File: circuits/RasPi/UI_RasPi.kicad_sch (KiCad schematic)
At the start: 14 parts, among them Q30 BSS138, Q33 BSS138

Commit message: 更新
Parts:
- removed Q30, Q33: BSS138, Package_TO_SOT_SMD:SOT-23, symbol Device:Q_NMOS_GSD
- added Q23, Q24: 2N7002, Package_TO_SOT_SMD:SOT-23, symbol Transistor_FET:2N7002
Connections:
- net GNDD: now also Q23.2 (S), Q24.2 (S)
- net LED_nG0: now also Q24.1 (G)
- net LED_nR0: now also Q23.1 (G)
- net at D23.2 (A), R113.2: now also Q24.3 (D)
- net at D29.2 (A), R120.2: now also Q23.3 (D)
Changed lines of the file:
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@@
   (junction (at 147.32 106.68) (diameter 0) (color 0 0 0 0)
   )
+  (junction (at 132.08 111.76) (diameter 0) (color 0 0 0 0)
+  )
+  (junction (at 147.32 116.84) (diameter 0) (color 0 0 0 0)
+  )
   (junction (at 177.8 111.76) (diameter 0) (color 0 0 0 0)
-  )
-  (junction (at 147.32 116.84) (diameter 0) (color 0 0 0 0)
-  )
-  (junction (at 132.08 111.76) (diameter 0) (color 0 0 0 0)
   )
   (junction (at 193.04 116.84) (diameter 0) (color 0 0 0 0)
@@
     )
   )
+  (symbol (lib_id "Transistor_FET:2N7002") (at 137.16 111.76 0) (unit 1)
+    (in_bom yes) (on_board yes) (dnp no)
+    (property "Reference" "Q23" (at 129.54 104.14 0)
+      (effects (font (size 1.27 1.27)) (justify left))
+    )
+    (property "Value" "2N7002" (at 129.54 106.68 0)
+      (effects (font (size 1.27 1.27)) (justify left))
+    )
+    (property "Footprint" "Package_TO_SOT_SMD:SOT-23" (at 142.24 113.665 0)
+      (effects (font (size 1.27 1.27) italic) (justify left) hide)
+    )
+    (property "Datasheet" "https://www.onsemi.com/pub/Collateral/NDS7002A-D.PDF" (at 142.24 115.57 0)
+      (effects (font (size 1.27 1.27)) (justify left) hide)
+    )
+    (pin "3")
+    (pin "1")
+    (pin "2")
+    (instances
+      (project "RasPi"
+        (path "/689a9e74-f202-4ea4-bfbb-4341f2549250/fddad0c3-2af8-46e3-8794-fa1122d24d51/69fce92a-28f6-4191-9f2f-418081756bee"
+          (reference "Q23") (unit 1)
+        )
+      )
+    )
+  )
   (symbol (lib_id "Device:LED") (at 193.04 111.76 90) (unit 1)
     (in_bom yes) (on_board yes) (dnp no)
@@
         (path "/689a9e74-f202-4ea4-bfbb-4341f2549250/fddad0c3-2af8-46e3-8794-fa1122d24d51/69fce92a-28f6-4191-9f2f-418081756bee"
           (reference "R120") (unit 1)
-        )
-      )
-    )
-  )
-  (symbol (lib_name "Q_NMOS_GSD_1") (lib_id "Device:Q_NMOS_GSD") (at 182.88 111.76 0) (unit 1)
-    (in_bom yes) (on_board yes) (dnp no)
-    (property "Reference" "Q30" (at 180.34 116.84 0)
-      (effects (font (size 1.27 1.27)) (justify left))
-    )
-    (property "Value" "BSS138" (at 180.34 119.38 0)
-      (effects (font (size 1.27 1.27)) (justify left))
-    )
-    (property "Footprint" "Package_TO_SOT_SMD:SOT-23" (at 187.96 109.22 0)
-      (effects (font (size 1.27 1.27)) hide)
-    )
-    (property "Datasheet" "~" (at 182.88 111.76 0)
-      (effects (font (size 1.27 1.27)) hide)
-    )
-    (pin "1")
-    (pin "2")
-    (pin "3")
-    (instances
-      (project "RasPi"
-        (path "/689a9e74-f202-4ea4-bfbb-4341f2549250/fddad0c3-2af8-46e3-8794-fa1122d24d51/69fce92a-28f6-4191-9f2f-418081756bee"
-          (reference "Q30") (unit 1)
         )
       )
@@
     )
   )
+  (symbol (lib_id "Transistor_FET:2N7002") (at 182.88 111.76 0) (unit 1)
+    (in_bom yes) (on_board yes) (dnp no)
+    (property "Reference" "Q24" (at 175.26 104.14 0)
+      (effects (font (size 1.27 1.27)) (justify left))
+    )
+    (property "Value" "2N7002" (at 175.26 106.68 0)
+      (effects (font (size 1.27 1.27)) (justify left))
+    )
+    (property "Footprint" "Package_TO_SOT_SMD:SOT-23" (at 187.96 113.665 0)
+      (effects (font (size 1.27 1.27) italic) (justify left) hide)
+    )
+    (property "Datasheet" "https://www.onsemi.com/pub/Collateral/NDS7002A-D.PDF" (at 187.96 115.57 0)
+      (effects (font (size 1.27 1.27)) (justify left) hide)
+    )
+    (pin "3")
+    (pin "1")
+    (pin "2")
+    (instances
+      (project "RasPi"
+        (path "/689a9e74-f202-4ea4-bfbb-4341f2549250/fddad0c3-2af8-46e3-8794-fa1122d24d51/69fce92a-28f6-4191-9f2f-418081756bee"
+          (reference "Q24") (unit 1)
+        )
+      )
+    )
+  )
   (symbol (lib_id "Device:R") (at 154.94 139.7 270) (mirror x) (unit 1)
     (in_bom yes) (on_board yes) (dnp no)
@@
         )
       )
-    )
-  )
-  (symbol (lib_name "Q_NMOS_GSD_1") (lib_id "Device:Q_NMOS_GSD") (at 137.16 111.76 0) (unit 1)
-    (in_bom yes) (on_board yes) (dnp no)
-    (property "Reference" "Q33" (at 134.62 116.84 0)
-      (effects (font (size 1.27 1.27)) (justify left))
-    )
-    (property "Value" "BSS138" (at 134.62 119.38 0)
-      (effects (font (size 1.27 1.27)) (justify left))
-    )
-    (property "Footprint" "Package_TO_SOT_SMD:SOT-23" (at 142.24 109.22 0)
-      (effects (font (size 1.27 1.27)) hide)
-    )
-    (property "Datasheet" "~" (at 137.16 111.76 0)
-      (effects (font (size 1.27 1.27)) hide)
-    )
-    (pin "1")
-    (pin "2")
-    (pin "3")
-    (instances
-      (project "RasPi"
-        (path "/689a9e74-f202-4ea4-bfbb-4341f2549250/fddad0c3-2af8-46e3-8794-fa1122d24d51/69fce92a-28f6-4191-9f2f-418081756bee"
-          (reference "Q33") (unit 1)
-        )
-      )

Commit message: raspi基板回路図
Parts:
- added D19, D28: Blue, LED_SMD:LED_0603_1608Metric_Pad1.05x0.95mm_HandSolder, symbol Device:LED
- added H7, H8: MountingHole_Pad, TestPoint:TestPoint_Pad_1.0x1.0mm, symbol Mechanical:MountingHole_Pad
- added R3, R42: 1k, Resistor_SMD:R_0402_1005Metric, symbol Device:R
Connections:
- net GNDD: now also D19.1 (K), D28.1 (K)
- new net: D28.2 (A), R42.1
- new net: D19.2 (A), R3.1
- new net LED_B0: H7.1, R3.2
- new net LED_B1: H8.1, R42.2
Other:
- note added: "LED"
- moved on the sheet: D23, D24, D25, D26, D29, Q23, Q24, R110, R111, R112, R113, R114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

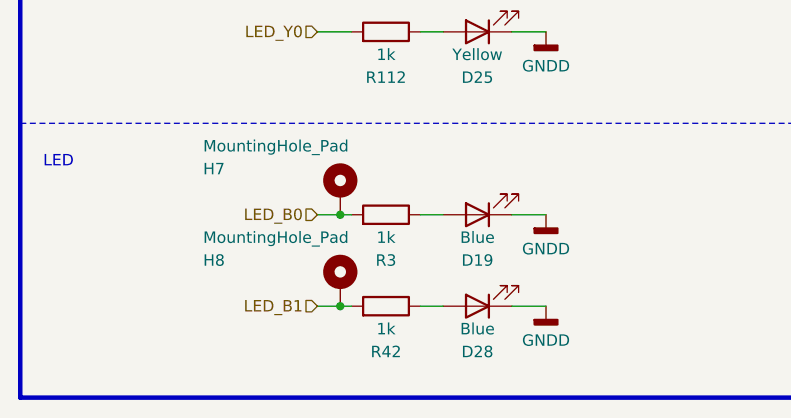
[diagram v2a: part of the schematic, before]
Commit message: 発注第2弾
RasPi発注
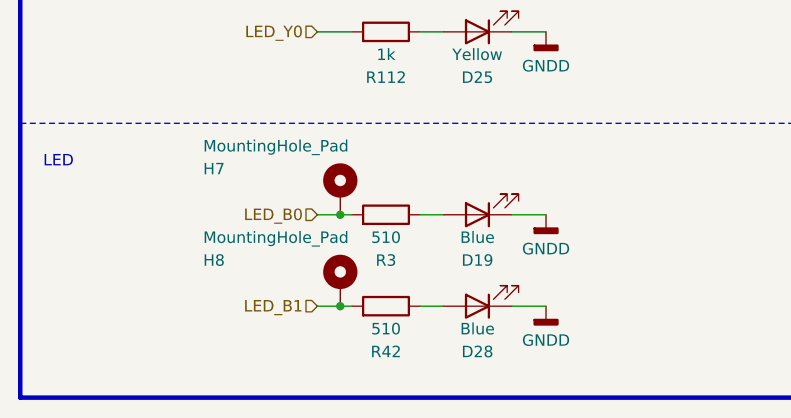
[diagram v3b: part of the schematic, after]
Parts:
- Q23, Q24: footprint Package_TO_SOT_SMD:SOT-23 -> Package_TO_SOT_SMD:SC-59
- R3, R42: value 1k -> 510
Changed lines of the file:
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@@
       (effects (font (size 1.27 1.27)))
     )
-    (property "Value" "1k" (at 152.4 144.78 90)
+    (property "Value" "510" (at 152.4 144.78 90)
       (effects (font (size 1.27 1.27)))
     )
@@
       (effects (font (size 1.27 1.27)) (justify left))
     )
-    (property "Footprint" "Package_TO_SOT_SMD:SOT-23" (at 139.7 95.885 0)
+    (property "Footprint" "Package_TO_SOT_SMD:SC-59" (at 139.7 95.885 0)
       (effects (font (size 1.27 1.27) italic) (justify left) hide)
     )
@@
       (effects (font (size 1.27 1.27)))
     )
-    (property "Value" "1k" (at 152.4 154.94 90)
+    (property "Value" "510" (at 152.4 154.94 90)
       (effects (font (size 1.27 1.27)))
     )
@@
       (effects (font (size 1.27 1.27)) (justify left))
     )
-    (property "Footprint" "Package_TO_SOT_SMD:SOT-23" (at 185.42 95.885 0)
+    (property "Footprint" "Package_TO_SOT_SMD:SC-59" (at 185.42 95.885 0)
       (effects (font (size 1.27 1.27) italic) (justify left) hide)
     )
